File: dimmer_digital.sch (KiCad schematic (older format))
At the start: 20 parts

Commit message: wiring up
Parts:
- gave numbers to parts that had none: 20
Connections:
- net at U1.3 (PB4): no longer R2.2
- net at U1.6 (PB1): now also R2.1, U3.5
- net 5V: now reaches U1.8 (VCC)
- net 5V: now also R2.2
- net at U3.1: now also D2.1 (K), D3.1 (K)
- net at U3.2: now also D4.2 (A), D5.2 (A)
- net GND: now reaches U3.4
- net at D2.2 (A): now also D4.1 (K), R4.2
- net at D3.2 (A): now also D5.1 (K), R5.2
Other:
- moved on the sheet: R2, U3
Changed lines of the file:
@@
 $EndDescr
 $Comp
-L MCU_Microchip_ATtiny:ATtiny13A-PU U?
+L MCU_Microchip_ATtiny:ATtiny13A-PU U1
 U 1 1 5E6B6DA8
 P 3900 1700
-F 0 "U?" H 3371 1746 50  0000 R CNN
+F 0 "U1" H 3371 1746 50  0000 R CNN
 F 1 "ATtiny13A-PU" H 3371 1655 50  0000 R CNN
 F 2 "Package_DIP:DIP-8_W7.62mm" H 3900 1700 50  0001 C CIN
@@
 $EndComp
 $Comp
-L Isolator:4N25 U?
+L Isolator:4N25 U3
 U 1 1 5E6B7772
-P 4950 2950
-F 0 "U?" H 4950 3275 50  0000 C CNN
-F 1 "4N25" H 4950 3184 50  0000 C CNN
-F 2 "Package_DIP:DIP-6_W7.62mm" H 4750 2750 50  0001 L CIN
-F 3 "https://www.vishay.com/docs/83725/4n25.pdf" H 4950 2950 50  0001 L CNN
-	1    4950 2950
-	1    0    0    -1
-$EndComp
-$Comp
-L Relay_SolidState:MOC3021M U?
+P 5600 1900
+F 0 "U3" H 5600 2225 50  0000 C CNN
+F 1 "4N25" H 5600 2134 50  0000 C CNN
+F 2 "Package_DIP:DIP-6_W7.62mm" H 5400 1700 50  0001 L CIN
+F 3 "https://www.vishay.com/docs/83725/4n25.pdf" H 5600 1900 50  0001 L CNN
+	1    5600 1900
+	-1   0    0    -1
+$EndComp
+$Comp
+L Relay_SolidState:MOC3021M U2
 U 1 1 5E6B8021
 P 5000 3850
-F 0 "U?" H 5000 4175 50  0000 C CNN
+F 0 "U2" H 5000 4175 50  0000 C CNN
 F 1 "MOC3021M" H 5000 4084 50  0000 C CNN
 F 2 "" H 4800 3650 50  0001 L CIN
@@
 $EndComp
 $Comp
-L Triac_Thyristor:TIC226 Q?
+L Triac_Thyristor:TIC226 Q1
 U 1 1 5E6B8A5E
 P 6300 3300
-F 0 "Q?" H 6429 3346 50  0000 L CNN
+F 0 "Q1" H 6429 3346 50  0000 L CNN
 F 1 "TIC226" H 6429 3255 50  0000 L CNN
 F 2 "Package_TO_SOT_THT:TO-220-3_Vertical" H 6500 3225 50  0001 L CIN
@@
 $EndComp
 $Comp
-L Diode:1N4004 D?
-U 1 1 5E6B95C0
-P 6250 1800
-F 0 "D?" H 6250 2016 50  0000 C CNN
-F 1 "1N4004" H 6250 1925 50  0000 C CNN
-F 2 "Diode_THT:D_DO-41_SOD81_P10.16mm_Horizontal" H 6250 1625 50  0001 C CNN
-F 3 "http://www.vishay.com/docs/88503/1n4001.pdf" H 6250 1800 50  0001 C CNN
-	1    6250 1800
-	1    0    0    -1
-$EndComp
-$Comp
-L Diode:1N4004 D?
-U 1 1 5E6BA42F
-P 6250 2150
-F 0 "D?" H 6250 2366 50  0000 C CNN
-F 1 "1N4004" H 6250 2275 50  0000 C CNN
-F 2 "Diode_THT:D_DO-41_SOD81_P10.16mm_Horizontal" H 6250 1975 50  0001 C CNN
-F 3 "http://www.vishay.com/docs/88503/1n4001.pdf" H 6250 2150 50  0001 C CNN
-	1    6250 2150
-	1    0    0    -1
-$EndComp
-$Comp
-L Diode:1N4004 D?
-U 1 1 5E6BA852
-P 6750 1800
-F 0 "D?" H 6750 2016 50  0000 C CNN
-F 1 "1N4004" H 6750 1925 50  0000 C CNN
-F 2 "Diode_THT:D_DO-41_SOD81_P10.16mm_Horizontal" H 6750 1625 50  0001 C CNN
-F 3 "http://www.vishay.com/docs/88503/1n4001.pdf" H 6750 1800 50  0001 C CNN
-	1    6750 1800
-	1    0    0    -1
-$EndComp
-$Comp
-L Diode:1N4004 D?
-U 1 1 5E6BAB65
-P 6750 2150
-F 0 "D?" H 6750 2366 50  0000 C CNN
-F 1 "1N4004" H 6750 2275 50  0000 C CNN
-F 2 "Diode_THT:D_DO-41_SOD81_P10.16mm_Horizontal" H 6750 1975 50  0001 C CNN
-F 3 "http://www.vishay.com/docs/88503/1n4001.pdf" H 6750 2150 50  0001 C CNN
-	1    6750 2150
-	1    0    0    -1
-$EndComp
-$Comp
-L Connector:Screw_Terminal_01x02 J?
+L Connector:Screw_Terminal_01x02 J1
 U 1 1 5E6BBA8A
 P 8200 1750
-F 0 "J?" H 8280 1742 50  0000 L CNN
+F 0 "J1" H 8280 1742 50  0000 L CNN
 F 1 "Screw_Terminal_01x02" H 8280 1651 50  0000 L CNN
 F 2 "" H 8200 1750 50  0001 C CNN
@@
 $EndComp
 $Comp
-L Connector:Screw_Terminal_01x02 J?
+L Connector:Screw_Terminal_01x02 J2
 U 1 1 5E6BC092
 P 8200 2650
-F 0 "J?" H 8280 2642 50  0000 L CNN
+F 0 "J2" H 8280 2642 50  0000 L CNN
 F 1 "Screw_Terminal_01x02" H 8280 2551 50  0000 L CNN
 F 2 "" H 8200 2650 50  0001 C CNN
@@
 $EndComp
 $Comp
-L Device:R R?
+L Device:R R4
 U 1 1 5E6BCA3F
 P 7400 1800
-F 0 "R?" V 7193 1800 50  0000 C CNN
+F 0 "R4" V 7193 1800 50  0000 C CNN
 F 1 "R" V 7284 1800 50  0000 C CNN
 F 2 "" V 7330 1800 50  0001 C CNN
@@
 $EndComp
 $Comp
-L Device:R R?
+L Device:R R5
 U 1 1 5E6BCF2F
 P 7400 2150
-F 0 "R?" V 7193 2150 50  0000 C CNN
+F 0 "R5" V 7193 2150 50  0000 C CNN
 F 1 "R" V 7284 2150 50  0000 C CNN
 F 2 "" V 7330 2150 50  0001 C CNN
@@
 $EndComp
 $Comp
-L Switch:SW_Push SW?
+L Switch:SW_Push SW1
 U 1 1 5E6BD9EF
 P 2750 1300
-F 0 "SW?" H 2750 1585 50  0000 C CNN
+F 0 "SW1" H 2750 1585 50  0000 C CNN
 F 1 "SW_Push" H 2750 1494 50  0000 C CNN
 F 2 "" H 2750 1500 50  0001 C CNN
@@
 $EndComp
 $Comp
-L Device:C C?
+L Device:C C1
 U 1 1 5E6C0439
 P 2550 1500
-F 0 "C?" H 2665 1546 50  0000 L CNN
+F 0 "C1" H 2665 1546 50  0000 L CNN
 F 1 "C" H 2665 1455 50  0000 L CNN
 F 2 "" H 2588 1350 50  0001 C CNN
@@
 $EndComp
 $Comp
-L Device:R_POT RV?
+L Device:R_POT RV1
 U 1 1 5E6C0B9B
 P 2600 2350
-F 0 "RV?" H 2531 2396 50  0000 R CNN
+F 0 "RV1" H 2531 2396 50  0000 R CNN
 F 1 "R_POT" H 2531 2305 50  0000 R CNN
 F 2 "" H 2600 2350 50  0001 C CNN
@@
 $EndComp
 $Comp
-L Device:R R?
+L Device:R R1
 U 1 1 5E6C1260
 P 3550 2800
-F 0 "R?" V 3343 2800 50  0000 C CNN
+F 0 "R1" V 3343 2800 50  0000 C CNN
 F 1 "R" V 3434 2800 50  0000 C CNN
 F 2 "" V 3480 2800 50  0001 C CNN
@@
 $EndComp
 $Comp
-L Device:LED D?
+L Device:LED D1
 U 1 1 5E6C193D
 P 4150 2800
-F 0 "D?" H 4143 2545 50  0000 C CNN
+F 0 "D1" H 4143 2545 50  0000 C CNN
 F 1 "LED" H 4143 2636 50  0000 C CNN
 F 2 "" H 4150 2800 50  0001 C CNN
@@
 $EndComp
 $Comp
-L Device:R R?
+L Device:R R3
 U 1 1 5E6C2071
 P 5700 3750
-F 0 "R?" V 5493 3750 50  0000 C CNN
+F 0 "R3" V 5493 3750 50  0000 C CNN
 F 1 "R" V 5584 3750 50  0000 C CNN
 F 2 "" V 5630 3750 50  0001 C CNN
@@
 	0    1    1    0
 $EndComp
-Wire Wire Line
-	4500 1800 4800 1800
-$Comp
-L Device:R R?
+$Comp
+L Device:R R2
 U 1 1 5E6C24CE
-P 4950 1800
-F 0 "R?" V 4743 1800 50  0000 C CNN
-F 1 "R" V 4834 1800 50  0000 C CNN
-F 2 "" V 4880 1800 50  0001 C CNN
-F 3 "~" H 4950 1800 50  0001 C CNN
-	1    4950 1800
-	0    1    1    0
-$EndComp
-$Comp
-L Converter_ACDC:HLK-PM03 PS?
+P 5050 1250
+F 0 "R2" V 4843 1250 50  0000 C CNN
+F 1 "R" V 4934 1250 50  0000 C CNN
+F 2 "" V 4980 1250 50  0001 C CNN
+F 3 "~" H 5050 1250 50  0001 C CNN
+	1    5050 1250
+	-1   0    0    1
+$EndComp
+$Comp
+L Converter_ACDC:HLK-PM03 PS1
 U 1 1 5E6EAC1E
 P 6200 1050
-F 0 "PS?" H 6200 1375 50  0000 C CNN
+F 0 "PS1" H 6200 1375 50  0000 C CNN
 F 1 "HLK-PM03" H 6200 1284 50  0000 C CNN
 F 2 "Converter_ACDC:Converter_ACDC_HiLink_HLK-PMxx" H 6200 750 50  0001 C CNN
@@
 	1    0    0    -1
 $EndComp
+Wire Wire Line
+	6400 2150 6500 2150
+Wire Wire Line
+	6500 1450 7250 1450
+Wire Wire Line
+	7250 1450 7250 1800
+Wire Wire Line
+	7250 2150 7250 2450
+Wire Wire Line
+	7250 2450 6500 2450
+Wire Wire Line
+	6500 2450 6500 2150
+Connection ~ 6500 2150
+Wire Wire Line
+	6500 2150 6600 2150
+Wire Wire Line
+	6500 1800 6400 1800
+Connection ~ 6500 1800
+Wire Wire Line
+	6500 1800 6500 1450
+Wire Wire Line
+	6600 1800 6500 1800
+$Comp
+L Diode:1N4004 D5
+U 1 1 5E6BAB65
+P 6750 2150
+F 0 "D5" H 6750 2366 50  0000 C CNN
+F 1 "1N4004" H 6750 2275 50  0000 C CNN
+F 2 "Diode_THT:D_DO-41_SOD81_P10.16mm_Horizontal" H 6750 1975 50  0001 C CNN
+F 3 "http://www.vishay.com/docs/88503/1n4001.pdf" H 6750 2150 50  0001 C CNN
+	1    6750 2150
+	1    0    0    -1
+$EndComp
+$Comp
+L Diode:1N4004 D4
+U 1 1 5E6BA852
+P 6750 1800
+F 0 "D4" H 6750 2016 50  0000 C CNN
+F 1 "1N4004" H 6750 1925 50  0000 C CNN
+F 2 "Diode_THT:D_DO-41_SOD81_P10.16mm_Horizontal" H 6750 1625 50  0001 C CNN
+F 3 "http://www.vishay.com/docs/88503/1n4001.pdf" H 6750 1800 50  0001 C CNN
+	1    6750 1800
+	1    0    0    -1
+$EndComp
+$Comp
+L Diode:1N4004 D3
+U 1 1 5E6BA42F
+P 6250 2150
+F 0 "D3" H 6250 2366 50  0000 C CNN
+F 1 "1N4004" H 6250 2275 50  0000 C CNN
+F 2 "Diode_THT:D_DO-41_SOD81_P10.16mm_Horizontal" H 6250 1975 50  0001 C CNN
+F 3 "http://www.vishay.com/docs/88503/1n4001.pdf" H 6250 2150 50  0001 C CNN
+	1    6250 2150
+	1    0    0    -1
+$EndComp
+$Comp
+L Diode:1N4004 D2
+U 1 1 5E6B95C0
+P 6250 1800
+F 0 "D2" H 6250 2016 50  0000 C CNN
+F 1 "1N4004" H 6250 1925 50  0000 C CNN
+F 2 "Diode_THT:D_DO-41_SOD81_P10.16mm_Horizontal" H 6250 1625 50  0001 C CNN
+F 3 "http://www.vishay.com/docs/88503/1n4001.pdf" H 6250 1800 50  0001 C CNN
+	1    6250 1800
+	1    0    0    -1
+$EndComp
+Wire Wire Line
+	6900 2150 6900 1800
+Wire Wire Line
+	6100 2150 6100 1800
+Wire Wire Line
+	6100 1800 5900 1800
+Connection ~ 6100 1800
+Wire Wire Line
+	6900 2150 6900 2350
+Wire Wire Line
+	6900 2350 5900 2350
+Wire Wire Line
+	5900 2350 5900 2000
+Connection ~ 6900 2150
+Wire Wire Line
+	5300 1900 5050 1900
+Text GLabel 4050 1000 2    50   UnSpc ~ 0
+5V
+Wire Wire Line
+	3900 1100 3900 1000
+Wire Wire Line
+	3900 1000 4050 1000
+Text GLabel 5050 1050 1    50   UnSpc ~ 0
+5V
+$Comp
+L power:GND #PWR01
+U 1 1 5E6E7F5C
+P 5050 2000
+F 0 "#PWR01" H 5050 1750 50  0001 C CNN
+F 1 "GND" H 5055 1827 50  0000 C CNN
+F 2 "" H 5050 2000 50  0001 C CNN
+F 3 "" H 5050 2000 50  0001 C CNN
+	1    5050 2000
+	1    0    0    -1
+$EndComp
+Wire Wire Line
+	5300 2000 5050 2000
+Wire Wire Line
+	5050 1050 5050 1100
+Wire Wire Line
+	4500 1500 5050 1500
+Wire Wire Line
+	5050 1900 5050 1500
+Wire Wire Line
+	5050 1500 5050 1400
+Connection ~ 5050 1500
 $EndSCHEMATC

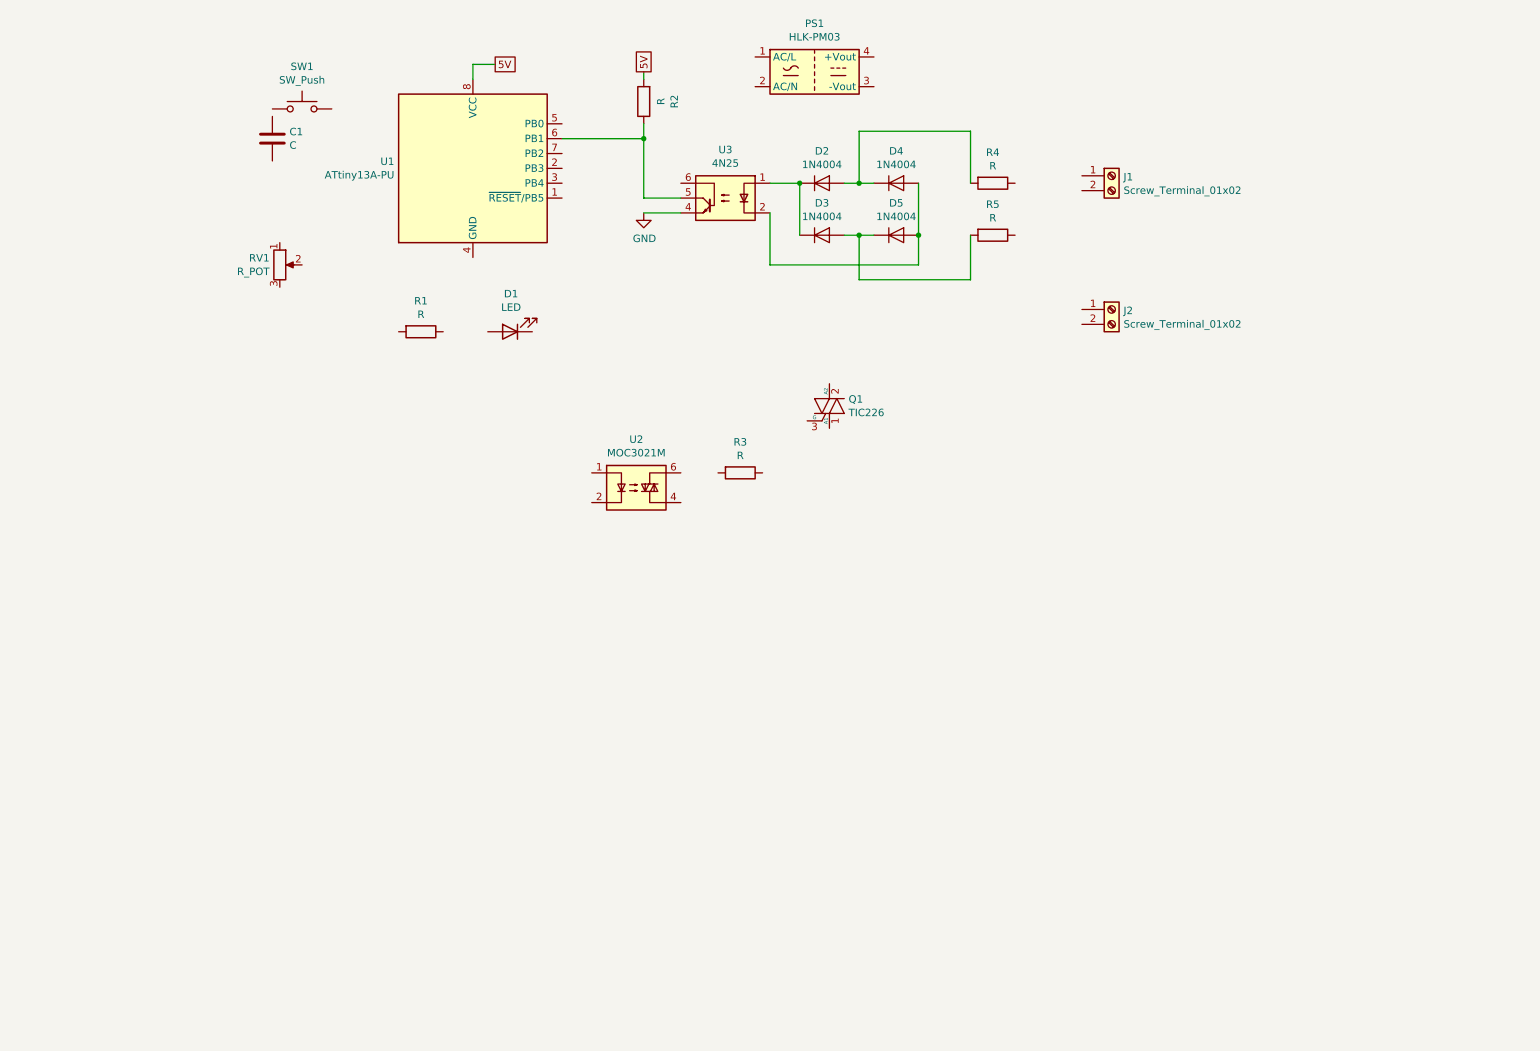
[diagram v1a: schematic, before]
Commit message: Updated components & wiring
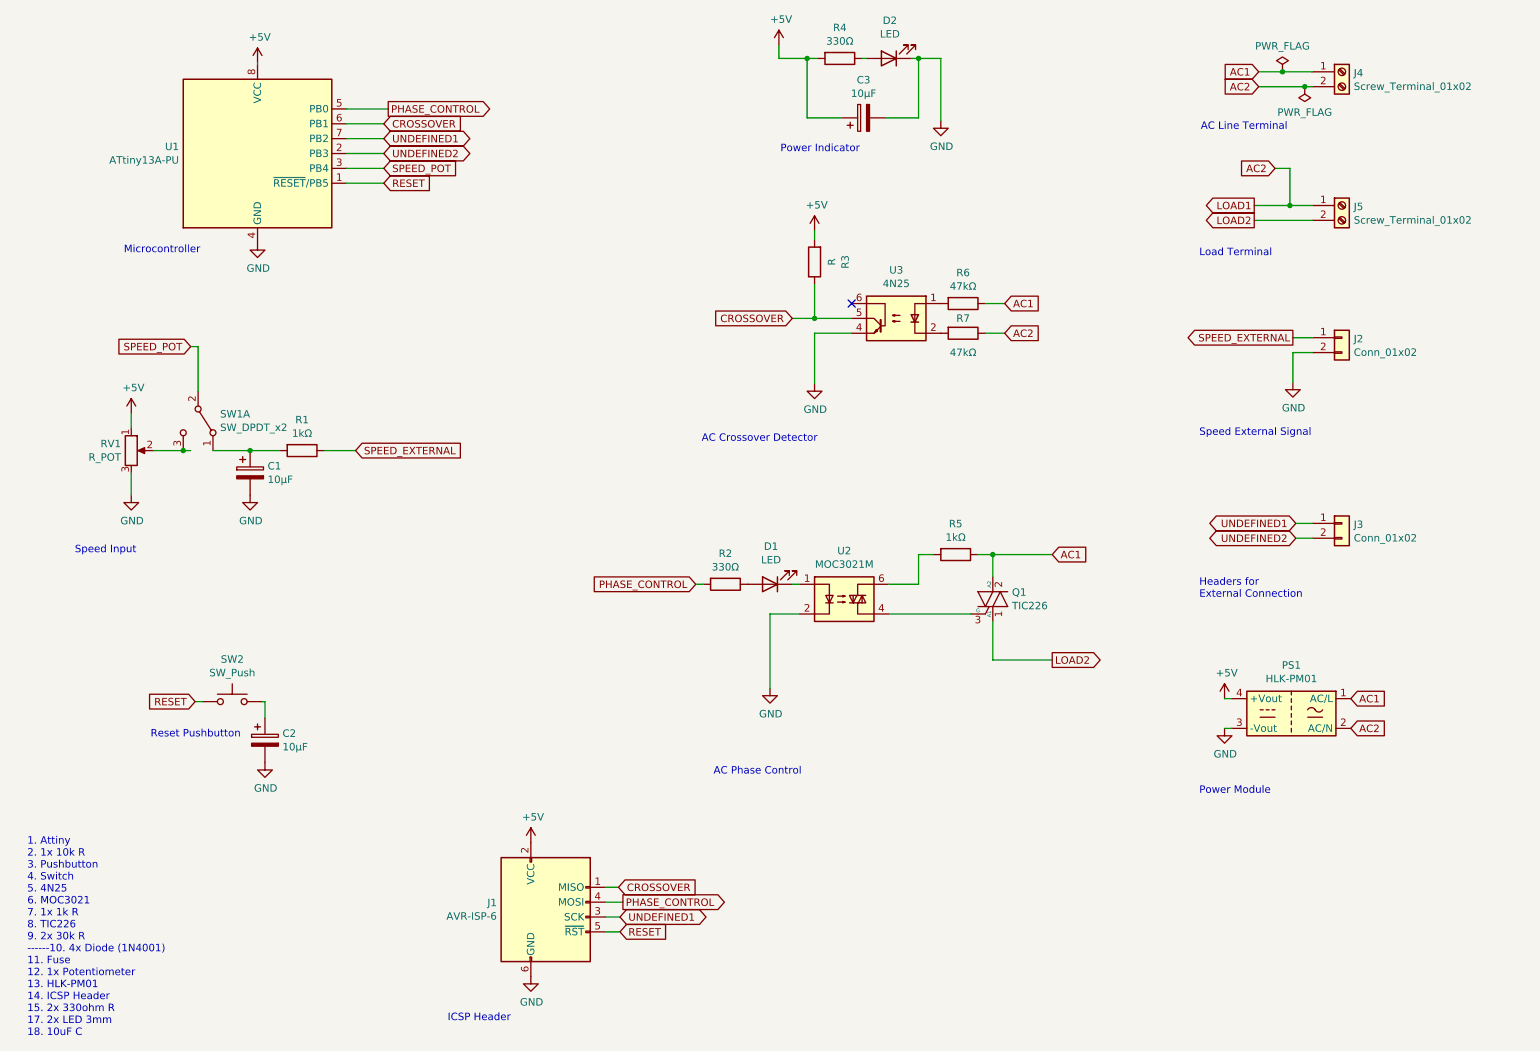
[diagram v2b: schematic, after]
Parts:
- removed C1: C, symbol Device:C
- removed D2, D3, D4, D5: 1N4004, Diode_THT:D_DO-41_SOD81_P10.16mm_Horizontal, symbol Diode:1N4004
- removed J1: Screw_Terminal_01x02, symbol Connector:Screw_Terminal_01x02
- removed PS1: HLK-PM03, Converter_ACDC:Converter_ACDC_HiLink_HLK-PMxx, symbol Converter_ACDC:HLK-PM03
- removed R3: R, symbol Device:R
- added C1, C2, C3: 10µF, symbol Device:CP
- added D2: LED, symbol Device:LED
- added J1: AVR-ISP-6, symbol Connector:AVR-ISP-6
- added J2, J3: Conn_01x02, symbol Connector_Generic:Conn_01x02
- added J4: Screw_Terminal_01x02, symbol Connector:Screw_Terminal_01x02
- added PS1: HLK-PM01, Converter_ACDC:Converter_ACDC_HiLink_HLK-PMxx, symbol Converter_ACDC:HLK-PM01
- added R2, R4: 330Ω, symbol Device:R
- added R5: 1kΩ, symbol Device:R
- added SW1: SW_DPDT_x2, symbol Switch:SW_DPDT_x2
- R1: value R -> 1kΩ
- R6: renamed from R4; value R -> 47kΩ
- R7: renamed from R5; value R -> 47kΩ
- renumbered J2 to J5, R2 to R3, SW1 to SW2
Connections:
- net 5V is gone; now on net +5V: R3.2, U1.8 (VCC)
- net GND: now also RV1.3, U1.4 (GND), U2.2, C1.2, C2.2, C3.2, D2.1 (K), J1.6 (GND), J2.2 (Pin_2), PS1.3 (-Vout)
- net RESET: now reaches U1.1 (~RESET~/PB5)
- net RESET: now also SW2.1, J1.5 (~RST)
- net UNDEFINED2: now reaches U1.2 (PB3)
- net UNDEFINED2: now also J3.2 (Pin_2)
- net SPEED_POT: now reaches U1.3 (PB4)
- net SPEED_POT: now also SW1.2 (B)
- net PHASE_CONTROL: now reaches U1.5 (PB0)
- net PHASE_CONTROL: now also J1.4 (MOSI), R2.2
- net CROSSOVER: now reaches R3.1, U1.6 (PB1), U3.5
- net CROSSOVER: now also J1.1 (MISO)
- net UNDEFINED1: now reaches U1.7 (PB2)
- net UNDEFINED1: now also J1.3 (SCK), J3.1 (Pin_1)
- net at U3.1: now also R6.2
- net at U3.2: now also R7.2
- net at U2.1: now also D1.1 (K)
- net at U2.4: now also Q1.3 (G)
- net at U2.6: now also R5.2
- net LOAD2: now reaches Q1.1 (A1)
- net LOAD2: now also J5.2 (Pin_2)
- net AC1: now reaches Q1.2 (A2)
- net AC1: now also R6.1, J4.1 (Pin_1), PS1.1 (AC/L), R5.1
- net AC2: now reaches J5.1 (Pin_1)
- net AC2: now also R7.1, J4.2 (Pin_2), PS1.2 (AC/N)
- net at SW2.2: now also C2.1
- net +5V: now reaches RV1.1
- net +5V: now also C3.1, J1.2 (VCC), PS1.4 (+Vout), R4.2
- net at RV1.2: now also SW1.3 (C)
- net SPEED_EXTERNAL: now reaches R1.1
- net SPEED_EXTERNAL: now also J2.1 (Pin_1)
- net at R1.2: now also C1.1, SW1.1 (A)
- net at D1.2 (A): now also R2.1
- new net: D2.2 (A), R4.1
- no-connect marks 0 -> 1
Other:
- note added: "1. Attiny\n2. 1x 10k R\n3. Pushbutton\n4. Switch\n5. 4N25\n6. MOC3021\n7. 1x 1k R\n8. TIC226\n9. 2x 30k R\n------10. 4x Diode (1N4001)\n11. Fuse\n12. 1x Potentiometer\n13. HLK-PM01\n14. ICSP Header\n15. 2x 330ohm R\n17. 2x LED 3mm\n18. 10uF C"
- note added: "AC Crossover Detector"
- note added: "AC Line Terminal"
- note added: "AC Phase Control"
- note added: "Headers for \nExternal Connection"
- note added: "ICSP Header"
- note added: "Load Terminal"
- note added: "Microcontroller"
- note added: "Power Indicator"
- note added: "Power Module"
- note added: "Reset Pushbutton\n"
- note added: "Speed External Signal"
- note added: "Speed Input"
- moved on the sheet: J5, R3, R6, R7, RV1, SW2, U1, U3
